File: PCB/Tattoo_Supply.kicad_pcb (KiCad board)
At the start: 2 copper layers, 140 parts, among them J1 Barrel_Jack_Switch, J2 Out_{1}, J3 Out_{2}, J4 USB_C_Receptacle_USB2.0, J5 Conn_ST_STDC14, J6 Debug_JTAG, J7 Debug_UART, J8 Footswitch, Q1 SiA441DJ, Q2 SSM6J507NU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

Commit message: ok better cap
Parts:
- C22, C23, C8, C9: footprint TattooSupplyFootprints:CPL_12.5_14 -> Capacitor_SMD:CP_Elec_8x10
- SW1: footprint Button_Switch_SMD:SW_SPST_Omron_B3FS-101xP -> Button_Switch_SMD:SW_SPST_EVQP2

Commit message: begin usb C
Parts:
- moved C34 246.9 mm to (261.5, 220.4)
- moved C7 246.9 mm to (242.6, 251.8)
- moved C8 246.9 mm to (228.9, 226.4)
- moved C9 246.9 mm to (228.9, 241.0)
- moved D13 246.9 mm to (267.2, 233.7)
- moved D6 246.9 mm to (251.5, 249.8)
- moved L1 246.9 mm to (247.8, 239.4)
- moved R13 246.9 mm to (255.5, 235.2)
- moved R14 246.9 mm to (255.5, 237.7)
- moved R43 246.9 mm to (261.5, 225.4)
- moved R44 246.9 mm to (261.5, 227.9)
- moved R46 246.9 mm to (261.5, 232.9)
- moved R47 246.9 mm to (261.5, 235.4)
- moved U2 246.9 mm to (248.1, 225.3)
- moved U8 246.9 mm to (270.4, 223.1)
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
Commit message: update dcdc 3V3 & begin routing
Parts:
- moved C23 176.2 mm to (126.2, 131.7), turned to 180 degrees
- moved C21 174.7 mm to (112.5, 120.9), turned to 180 degrees
- moved D7 161.6 mm to (103.6, 123.0), turned to 180 degrees
- moved C22 157.5 mm to (126.2, 146.3), turned to 180 degrees
- moved L2 151.1 mm to (109.2, 133.2), turned to 180 degrees
- moved R28 141.2 mm to (99.6, 132.5), turned to 180 degrees
- moved R27 136.9 mm to (99.6, 135.0), turned to 180 degrees
- moved R26 132.7 mm to (99.6, 137.5), turned to 180 degrees
- moved C10 129.5 mm to (172.2, 133.6)
- moved C34 129.5 mm to (178.3, 121.2)
- moved C7 129.5 mm to (159.3, 152.7)
- moved C8 129.5 mm to (145.7, 127.3)
- moved C9 129.5 mm to (145.7, 141.9)
- moved D13 129.5 mm to (184.0, 134.6)
- moved D6 129.5 mm to (168.3, 150.6)
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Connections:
- C27 pad 1: Net-(U5-BST) -> Net-(D9-K)
- D9 pad 1: Net-(D8-K) -> Net-(D9-K)
- U5 pad 1: Net-(U5-BST) -> Net-(D9-K)
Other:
- copper layers 2 -> 4

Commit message: Update Tattoo_Supply.kicad_pcb
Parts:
- moved C9 79.5 mm to (223.5, 126.0), turned to 90 degrees
- moved C8 68.7 mm to (214.4, 126.0), turned to 90 degrees
- moved C7 65.9 mm to (205.0, 105.2), turned to 90 degrees
- moved C34 58.9 mm to (235.9, 108.9)
- moved D12 58.9 mm to (242.0, 118.0)
- moved Q4 58.9 mm to (247.8, 122.5)
- moved R42 58.9 mm to (235.9, 111.4)
- moved R43 58.9 mm to (235.9, 114.0)
- moved R44 58.9 mm to (235.9, 116.5)
- moved R45 58.9 mm to (235.9, 119.0)
- moved R46 58.9 mm to (235.9, 121.5)
- moved R47 58.9 mm to (235.9, 124.0)
- moved U2 58.9 mm to (222.5, 113.9)
- moved U8 58.9 mm to (244.8, 111.7)
- moved D13 58.9 mm to (241.6, 122.3)
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
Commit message: first architecture
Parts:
- moved Q4 144.5 mm to (106.7, 154.0)
- moved D13 139.5 mm to (108.9, 165.3), turned to 180 degrees
- moved R45 136.6 mm to (103.8, 154.0), turned to -90 degrees
- moved R44 135.9 mm to (104.5, 151.4)
- moved U8 135.7 mm to (115.6, 153.1), turned to 90 degrees
- moved D12 134.8 mm to (115.8, 165.3)
- moved R42 131.4 mm to (105.4, 126.6)
- moved R46 130.4 mm to (109.8, 154.8), turned to -90 degrees
- moved C34 128.5 mm to (108.4, 125.0)
- moved R43 128.1 mm to (108.4, 126.6)
- moved R47 124.9 mm to (116.7, 161.3), turned to -90 degrees
- moved H2 106.9 mm to (170.7, 51.7)
- moved C7 91.4 mm to (115.7, 124.7)
- moved C8 91.4 mm to (125.1, 145.6)
- moved C9 91.4 mm to (134.2, 145.5)
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
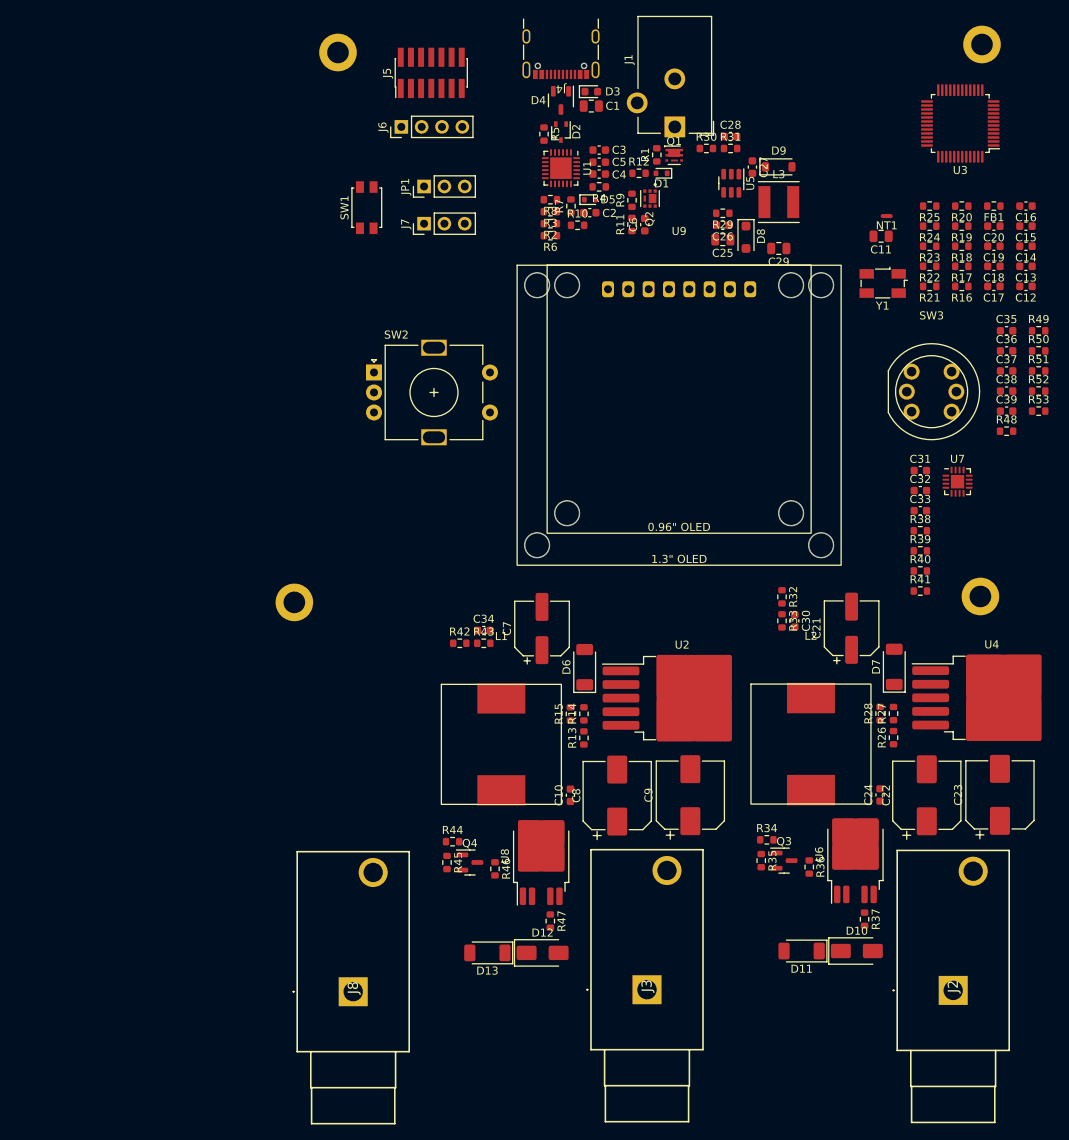
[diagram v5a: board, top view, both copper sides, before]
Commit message: good second placement
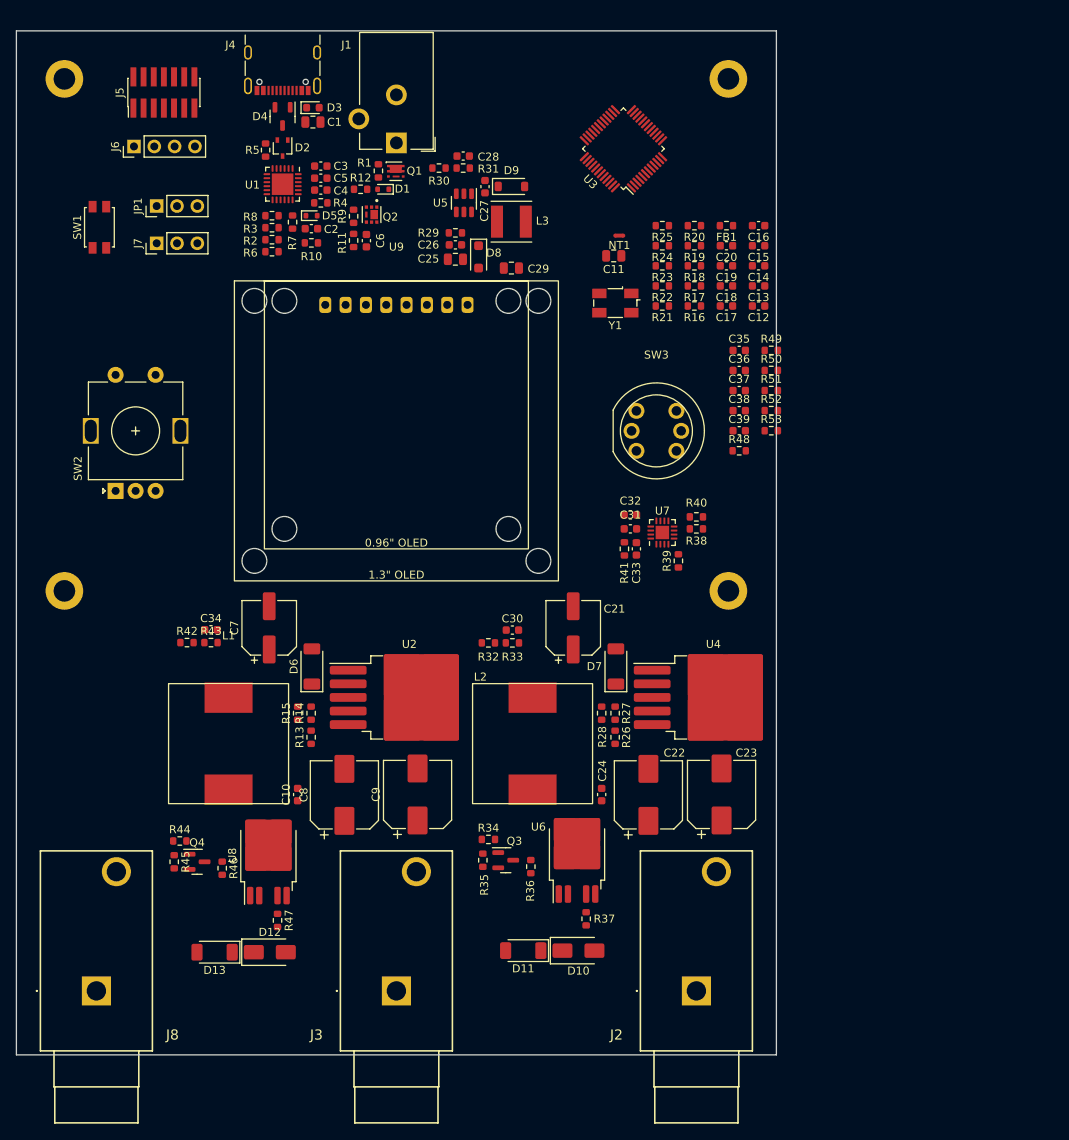
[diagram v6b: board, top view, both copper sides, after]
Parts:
- moved U3 42.2 mm to (125.9, 64.7), turned to 135 degrees
- moved U7 37.4 mm to (130.8, 112.7), turned to 90 degrees
- moved R41 37.4 mm to (126.0, 114.8), turned to -90 degrees
- moved R32 37.1 mm to (109.0, 126.5), turned to 0 degrees
- moved C31 37.0 mm to (126.8, 112.2)
- moved C32 36.4 mm to (126.8, 110.5), turned to 180 degrees
- moved C33 35.8 mm to (127.5, 114.8), turned to -90 degrees
- moved SW2 35.5 mm to (62.4, 107.5), turned to 90 degrees
- moved U9 35.4 mm to (97.5, 100.0)
- moved C30 35.3 mm to (112.0, 124.9), turned to 0 degrees
- moved C6 34.9 mm to (93.8, 76.2)
- moved D1 34.9 mm to (95.8, 69.8)
- moved D5 34.9 mm to (86.9, 73.1)
- moved J1 34.9 mm to (97.5, 64.0)
- moved R1 34.9 mm to (95.2, 67.5)
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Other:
- board outline added: 95 x 128 mm

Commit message: placement ok
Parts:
- moved R50 101.0 mm to (60.0, 148.0), turned to 180 degrees
- moved C37 97.4 mm to (60.0, 150.0), turned to 180 degrees
- moved R49 80.9 mm to (66.6, 112.5)
- moved C35 79.9 mm to (63.2, 110.5), turned to 180 degrees
- moved R51 79.7 mm to (65.0, 87.5), turned to 180 degrees
- moved R48 77.8 mm to (63.2, 112.5)
- moved C36 75.9 mm to (66.6, 110.5), turned to 180 degrees
- moved C38 75.7 mm to (65.0, 90.0), turned to 180 degrees
- moved C17 24.5 mm to (120.5, 68.1)
- moved R23 21.0 mm to (120.5, 61.0)
- moved C14 20.1 mm to (131.0, 63.1), turned to 0 degrees
- moved R21 18.6 mm to (136.0, 66.5)
- moved R24 17.6 mm to (120.5, 62.5)
- moved R22 17.2 mm to (134.0, 65.0)
- moved NT1 16.2 mm to (141.0, 71.3), turned to 90 degrees
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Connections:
- Y1 pad 2: Net-(C16-Pad1) -> GND
- Y1 pad 3: (no net) -> Net-(C16-Pad1)
- Y1 pad 4: (no net) -> GND

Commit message: begin routing
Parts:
- moved C25 0.88 mm to (104.0, 78.5)
- moved C26 0.88 mm to (104.0, 76.7)
- moved R29 0.88 mm to (104.0, 75.2)
- moved C27 0.22 mm to (108.4, 69.6)
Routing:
- net Net-(U1-DISCH): track 0.00 -> 15.8 mm, vias 0 -> 2
- net /USB C Power Delivery/2V7: track 0.00 -> 12.4 mm, vias 0 -> 2
- net Net-(Q2-G): track 0.00 -> 12.3 mm, vias 0 -> 2
- net /USB C Power Delivery/CC1: track 0.00 -> 11.3 mm
- net /USB C Power Delivery/CC2: track 0.00 -> 11.3 mm
- net Net-(U1-ADDR0): track 0.00 -> 8.47 mm
- net Net-(U1-VBUS_EN_SNK): track 0.00 -> 7.21 mm
- net GND: track 0.00 -> 6.21 mm, vias 0 -> 3
- net Net-(D5-K): track 0.00 -> 5.27 mm
- net Net-(D9-K): track 0.00 -> 4.25 mm
- net Net-(U1-ADDR1): track 0.00 -> 3.85 mm
- net Net-(U5-EN): track 0.00 -> 3.36 mm
- net Net-(D1-A): track 0.00 -> 2.82 mm
- net Net-(#FLG01-pwr): track 0.00 -> 2.46 mm
- net Net-(U1-VREG_1V2): track 0.00 -> 2.24 mm
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- added copper zone on F.Cu, net +3V3
- added copper zone on In2.Cu, net GND
- added copper zone on F.Cu, net Net-(D8-K)
- added copper zone on F.Cu, net Net-(Q1-D)
